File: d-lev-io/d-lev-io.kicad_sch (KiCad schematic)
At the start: 29 parts, among them J1 PJ-059A, J2 USB_C_Receptacle_USB2.0, J8 Conn_01x12_MountingPin, U1 AP1117-ADJ

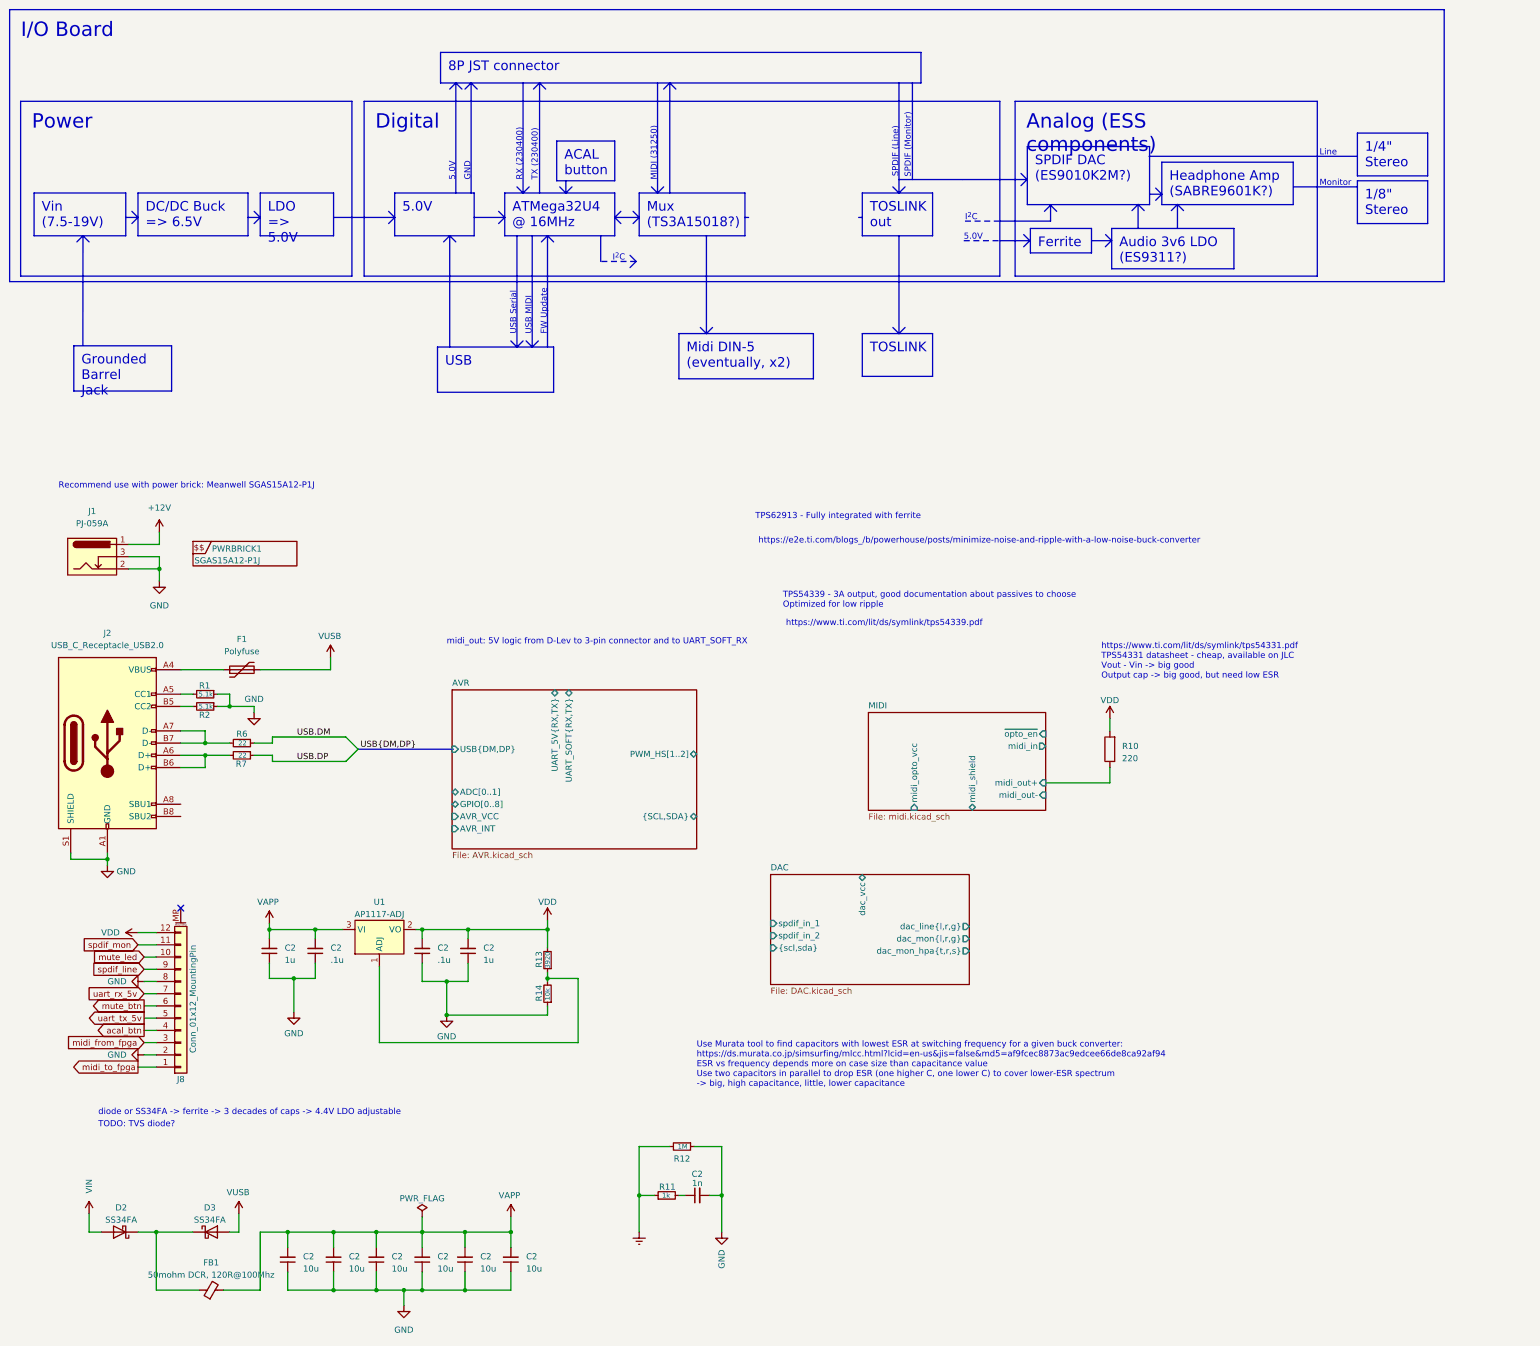
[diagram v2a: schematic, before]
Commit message: Add buck converter schematic
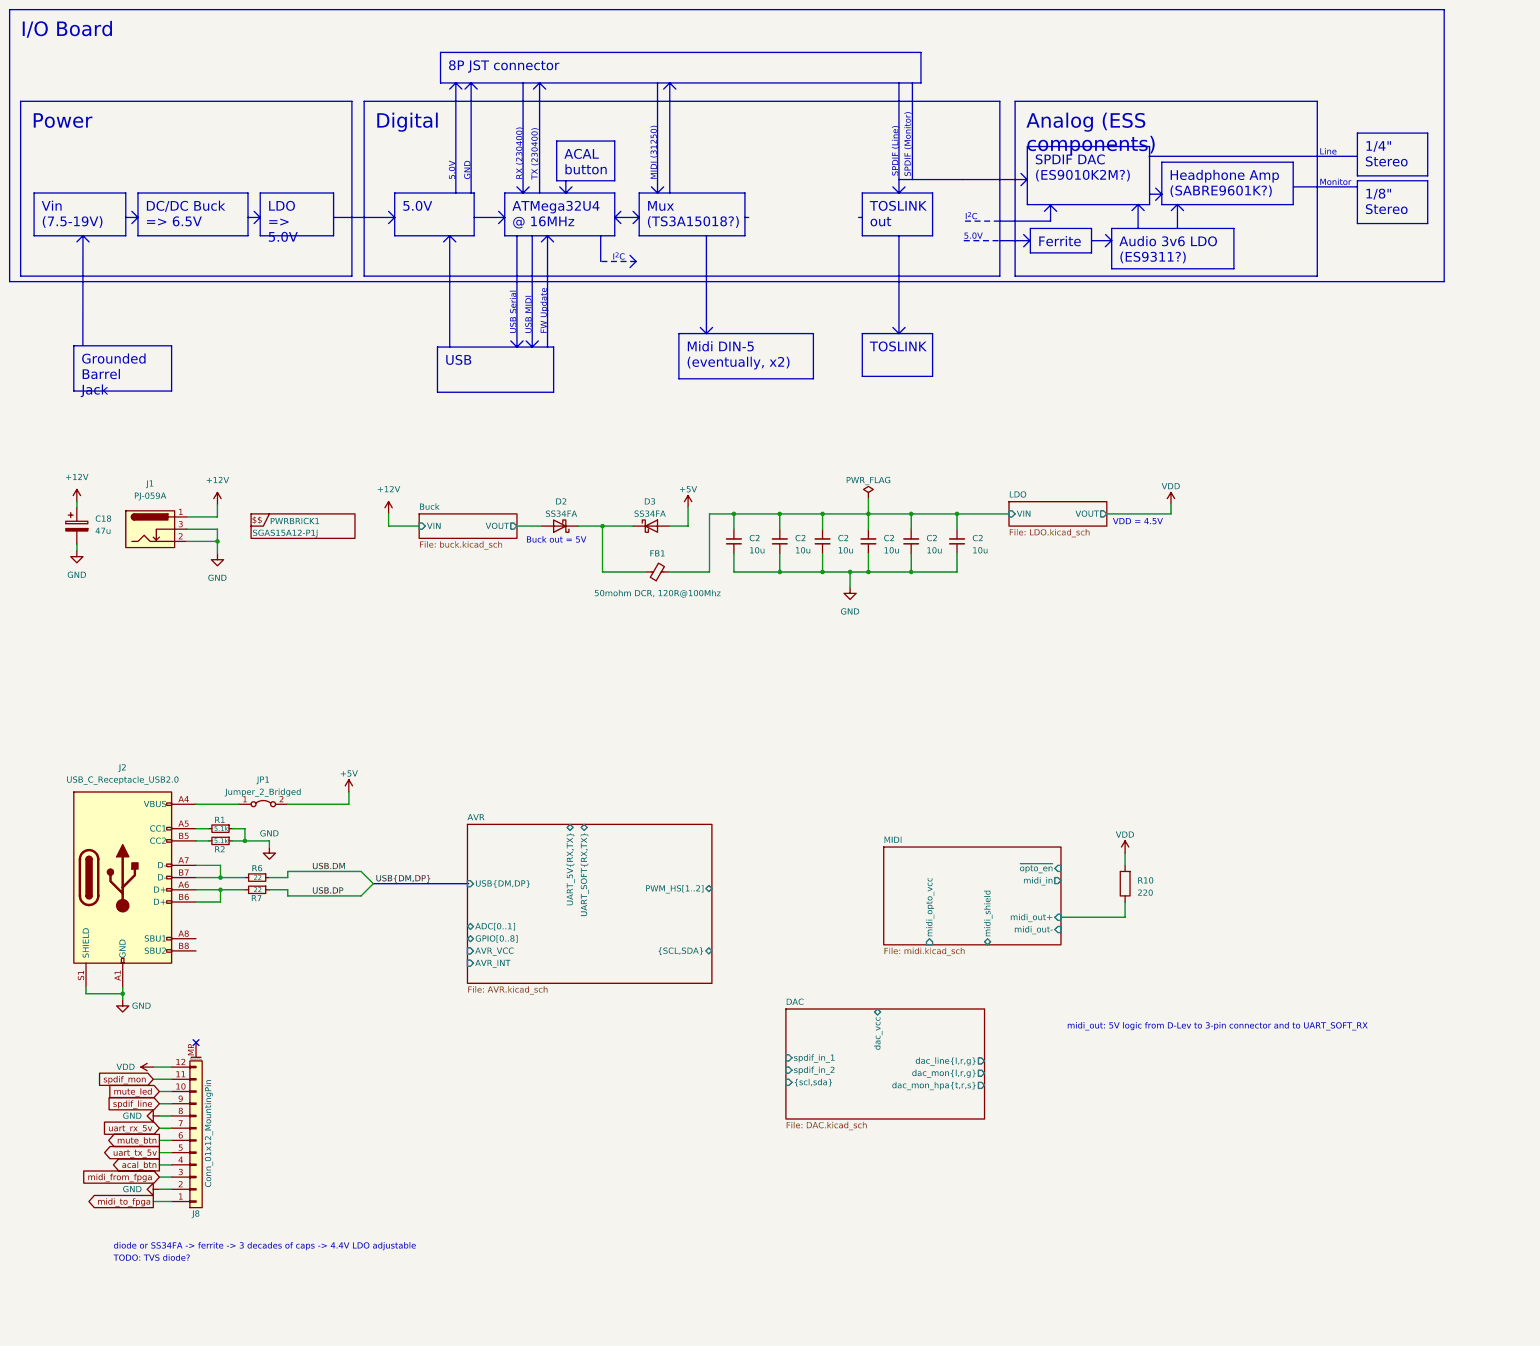
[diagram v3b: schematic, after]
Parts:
- removed C2 (x2): .1u, symbol Device:C_Small
- removed C2 (x2): 1u, symbol Device:C_Small
- removed C2: 1n, symbol Device:C_Small
- removed F1: Polyfuse, symbol Device:Polyfuse
- removed R11: 1k, Resistor_SMD:R_0805_2012Metric_Pad1.20x1.40mm_HandSolder, symbol Device:R_Small
- removed R12: 1M, Resistor_SMD:R_0805_2012Metric_Pad1.20x1.40mm_HandSolder, symbol Device:R_Small
- removed R13: 3920, Resistor_SMD:R_0805_2012Metric_Pad1.20x1.40mm_HandSolder, symbol Device:R_Small
- removed R14: 10k, Resistor_SMD:R_0805_2012Metric_Pad1.20x1.40mm_HandSolder, symbol Device:R_Small
- removed U1: AP1117-ADJ, Package_TO_SOT_SMD:SOT-223-3_TabPin2, symbol Regulator_Linear:AP1117-ADJ
- added C18: 47u, symbol Device:C_Polarized
- added JP1: Jumper_2_Bridged, symbol Jumper:Jumper_2_Bridged
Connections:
- net +12V: now also C18.1
- net +5V: now also D3.2 (A), JP1.2 (B); no longer D2.2 (A)
- net GND: now also C18.2
- net at J2.A4 (VBUS), J2.A9 (VBUS), J2.B4 (VBUS)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: now also JP1.1 (A)
- net VBUS renamed LDO/VIN
- net LDO/VIN: no longer D3.2 (A)
- new net Buck/VOUT: D2.2 (A)
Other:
- added sheet Buck (buck.kicad_sch)
- added sheet LDO (LDO.kicad_sch)
- note added: "Buck out = 5V"
- note added: "VDD = 4.5V"
- note removed: "Recommend use with power brick: Meanwell SGAS15A12-P1J"
- note removed: "TPS54339 - 3A output, good documentation about passives to choose Optimized for low ripple"
- note removed: "TPS62913 - Fully integrated with ferrite"
- note removed: "Use Murata tool to find capacitors with lowest ESR at switching frequency for a given buck converter: https://ds.murata.co.jp/simsurfing/mlcc.html?lcid=en-us&jis=false&md5=af9fcec8873ac9edcee66de8ca92af94 ESR vs frequency depends more on case size than capacitance value Use two capacitors in parallel to drop ESR (one higher C, one lower C) to cover lower-ESR spectrum -> big, high capacitance, lit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"
- note removed: "https://e2e.ti.com/blogs_/b/powerhouse/posts/minimize-noise-and-ripple-with-a-low-noise-buck-converter"
- note removed: "https://www.ti.com/lit/ds/symlink/tps54331.pdf TPS54331 datasheet - cheap, available on JLC Vout - Vin -> big good Output cap -> big good, but need low ESR"
- note removed: "https://www.ti.com/lit/ds/symlink/tps54339.pdf"
- moved on the sheet: C2, D2, D3, FB1, J1, J2, J8, PWRBRICK1, R1, R10, R2, R6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

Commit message: many many changes'
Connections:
- net midi_from_fpga renamed midi_from_fpga_3v
- net midi_to_fpga renamed midi_to_fpga_3v
- net uart_rx_5v renamed uart_rx_3v
- net uart_tx_5v renamed uart_tx_3v
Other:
- sheet LDO renamed LDO4V5
- added sheet LDO3v3 (LDO.kicad_sch)
- sheet AVR ports: added UART_AVR{RX,TX}; removed UART_5V{RX,TX}
- sheet LDO4V5: file LDO.kicad_sch -> LDO4v5.kicad_sch
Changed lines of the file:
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@@
   (junction (at 203.2 23.495) (diameter 0) (color 0 0 0 0)
+  )
+  (junction (at 247.65 23.495) (diameter 0) (color 0 0 0 0)
   )
   (junction (at 156.845 23.495) (diameter 0) (color 0 0 0 0)
@@
     (stroke (width 0) (type default))
   )
+  (wire (pts (xy 247.65 23.495) (xy 256.54 23.495))
+    (stroke (width 0) (type default))
+  )
   (wire (pts (xy 64.135 101.6) (xy 64.135 102.87))
     (stroke (width 0) (type default))
@@
     (stroke (width 0) (type dash))
   )
+  (wire (pts (xy 280.67 22.225) (xy 280.67 23.495))
+    (stroke (width 0) (type default))
+  )
   (wire (pts (xy 20.32 22.225) (xy 20.32 20.955))
     (stroke (width 0) (type default))
@@
   )
   (wire (pts (xy 234.315 23.495) (xy 247.65 23.495))
+    (stroke (width 0) (type default))
+  )
+  (wire (pts (xy 280.67 23.495) (xy 272.415 23.495))
     (stroke (width 0) (type default))
   )
@@
     )
   )
-  (global_label "midi_to_fpga" (shape output) (at 36.195 166.37 180) (fields_autoplaced)
+  (global_label "midi_to_fpga_3v" (shape output) (at 36.195 166.37 180) (fields_autoplaced)
     (effects (font (size 1.27 1.27)) (justify right))
-    (property "Intersheetrefs" "${INTERSHEET_REFS}" (at 22.5247 151.13 0)
+    (property "Intersheetrefs" "${INTERSHEET_REFS}" (at 18.11 166.37 0)
       (effects (font (size 1.27 1.27)) (justify right) hide)
     )
@@
     )
   )
-  (global_label "uart_tx_5v" (shape output) (at 37.465 156.21 180) (fields_autoplaced)
+  (global_label "uart_tx_3v" (shape output) (at 37.465 156.21 180) (fields_autoplaced)
     (effects (font (size 1.27 1.27)) (justify right))
-    (property "Intersheetrefs" "${INTERSHEET_REFS}" (at 24.8832 146.05 0)
+    (property "Intersheetrefs" "${INTERSHEET_REFS}" (at 24.8832 156.21 0)
       (effects (font (size 1.27 1.27)) (justify right) hide)
     )
   )
-  (global_label "uart_rx_5v" (shape input) (at 37.465 151.13 180) (fields_autoplaced)
+  (global_label "uart_rx_3v" (shape input) (at 37.465 151.13 180) (fields_autoplaced)
     (effects (font (size 1.27 1.27)) (justify right))
-    (property "Intersheetrefs" "${INTERSHEET_REFS}" (at 24.8227 143.51 0)
+    (property "Intersheetrefs" "${INTERSHEET_REFS}" (at 24.8227 151.13 0)
       (effects (font (size 1.27 1.27)) (justify right) hide)
     )
   )
-  (global_label "midi_from_fpga" (shape input) (at 37.465 161.29 180) (fields_autoplaced)
+  (global_label "midi_from_fpga_3v" (shape input) (at 37.465 161.29 180) (fields_autoplaced)
     (effects (font (size 1.27 1.27)) (justify right))
-    (property "Intersheetrefs" "${INTERSHEET_REFS}" (at 20.0452 148.59 0)
+    (property "Intersheetrefs" "${INTERSHEET_REFS}" (at 16.9005 161.29 0)
       (effects (font (size 1.27 1.27)) (justify right) hide)
     )
@@
     )
   )
+  (symbol (lib_id "power:+3V3") (at 280.67 22.225 0) (unit 1)
+    (in_bom yes) (on_board yes) (dnp no)
+    (property "Reference" "#PWR031" (at 280.67 26.035 0)
+      (effects (font (size 1.27 1.27)) hide)
+    )
+    (property "Value" "+3V3" (at 280.67 17.145 0)
+      (effects (font (size 1.27 1.27)))
+    )
+    (property "Footprint" "" (at 280.67 22.225 0)
+      (effects (font (size 1.27 1.27)) hide)
+    )
+    (property "Datasheet" "" (at 280.67 22.225 0)
+      (effects (font (size 1.27 1.27)) hide)
+    )
+    (pin "1")
+    (instances
+      (project "d-lev-io"
+        (path "/9261a07b-ae4a-4d72-8042-ea097cd0e5ed"
+          (reference "#PWR031") (unit 1)
+        )
+      )
+    )
+  )
   (symbol (lib_id "power:GND") (at 37.465 148.59 270) (unit 1)
     (in_bom yes) (on_board yes) (dnp no)
@@
     )
   )
+  (sheet (at 256.54 21.59) (size 15.875 3.81) (fields_autoplaced)
+    (stroke (width 0.1524) (type solid))
+    (fill (color 0 0 0 0.0000))
+    (property "Sheetname" "LDO3v3" (at 256.54 20.8784 0)
+      (effects (font (size 1.27 1.27)) (justify left bottom))
+    )
+    (property "Sheetfile" "LDO.kicad_sch" (at 256.54 25.9846 0)
+      (effects (font (size 1.27 1.27)) (justify left top))
+    )
+    (pin "VIN" input (at 256.54 23.495 180)
+      (effects (font (size 1.27 1.27)) (justify left))
+    )
+    (pin "VOUT" output (at 272.415 23.495 0)
+      (effects (font (size 1.27 1.27)) (justify right))
+    )
+    (instances
+      (project "d-lev-io"
+        (path "/9261a07b-ae4a-4d72-8042-ea097cd0e5ed" (page "8"))
+      )
+    )
+  )
   (sheet (at 101.473 88.011) (size 50.8 33.02) (fields_autoplaced)
     (stroke (width 0.1524) (type solid))
@@
       (effects (font (size 1.27 1.27)) (justify left))
     )
-    (pin "UART_5V{RX,TX}" bidirectional (at 122.809 88.011 90)
+    (pin "UART_AVR{RX,TX}" bidirectional (at 122.809 88.011 90)
       (effects (font (size 1.27 1.27)) (justify right))
     )
@@
     (stroke (width 0.1524) (type solid))
     (fill (color 0 0 0 0.0000))
-    (property "Sheetname" "LDO" (at 213.995 20.2434 0)
+    (property "Sheetname" "LDO4V5" (at 213.995 20.2434 0)
       (effects (font (size 1.27 1.27)) (justify left bottom))
     )
-    (property "Sheetfile" "LDO.kicad_sch" (at 213.995 26.6196 0)
+    (property "Sheetfile" "LDO4v5.kicad_sch" (at 213.995 26.6196 0)
       (effects (font (size 1.27 1.27)) (justify left top))
     )

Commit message: many more changes
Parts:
- removed R10: 220, Resistor_SMD:R_0603_1608Metric, symbol Device:R
- added J4: MIDI_OUT_JACK, Connector_Audio:Jack_3.5mm_CUI_SJ-3523-SMT_Horizontal, symbol Connector:AudioJack3
- added R18: 10, Resistor_SMD:R_0603_1608Metric, symbol Device:R_Small
- added R8: 33, Resistor_SMD:R_0603_1608Metric, symbol Device:R_Small
- added TP1: VIN, TestPoint:TestPoint_Pad_D1.5mm, symbol Connector:TestPoint
- added TP2: VUSB, TestPoint:TestPoint_Pad_D1.5mm, symbol Connector:TestPoint
- added TP3: VDD, TestPoint:TestPoint_Pad_D1.5mm, symbol Connector:TestPoint
- added TP4: VSYS, TestPoint:TestPoint_Pad_D1.5mm, symbol Connector:TestPoint
- added TP5: GND, TestPoint:TestPoint_Pad_D1.5mm, symbol Connector:TestPoint
- added U6: 74AHC1G126, Package_TO_SOT_SMD:SOT-23-5, symbol 74xGxx:74AHC1G126
- C1: renamed from C18; footprint (none) -> Capacitor_SMD:C_1206_3216Metric
- C2: footprint (none) -> Capacitor_SMD:C_0805_2012Metric
- D1: renamed from D2; footprint (none) -> Diode_SMD:D_SOD-123F
- D2: renamed from D3; footprint (none) -> Diode_SMD:D_SOD-123F
- FB1: footprint Inductor_SMD:L_0201_0603Metric -> Inductor_SMD:L_0603_1608Metric
- J3: renamed from J8; symbol Connector_Generic_MountingPin:Conn_01x12_MountingPin -> assorted:Conn_01x12_MountingPin
- JP1: footprint (none) -> Jumper:SolderJumper-2_P1.3mm_Bridged_RoundedPad1.0x1.5mm
- R1, R2: footprint Resistor_SMD:R_0805_2012Metric_Pad1.20x1.40mm_HandSolder -> Resistor_SMD:R_0603_1608Metric
- R3: renamed from R6; footprint Resistor_SMD:R_0805_2012Metric_Pad1.20x1.40mm_HandSolder -> Resistor_SMD:R_0603_1608Metric
- R4: renamed from R7; footprint Resistor_SMD:R_0805_2012Metric_Pad1.20x1.40mm_HandSolder -> Resistor_SMD:R_0603_1608Metric
- renumbered J2 to J1, J1 to J2
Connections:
- net LDO4V5/VIN is gone; now on net +5V: C2.2, C2.2, C2.2, C2.2, C2.2, C2.2, FB1.2
- net +12V: now also TP1.1
- net +3V3: now also R8.1, TP4.1, U6.1, U6.5 (VCC)
- net +5V: now also TP3.1; no longer D2.2 (A), JP1.2 (B)
- net GND: now also J4.S, TP5.1, U6.3 (GND)
- net midi_from_fpga_3v: now also U6.2
- new net: R18.1, U6.4
- new net: J4.R, R8.2
- new net: J4.T, R18.2
- new net VBUS: D2.2 (A), JP1.2 (B), TP2.1
- no-connect marks 1 -> 3
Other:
- removed sheet LDO4V5
- removed sheet MIDI
- sheet AVR ports: added PWM_16BIT[1..2], UART_AVR_RX, UART_AVR_SOFT_RX, UART_AVR_SOFT_TX, UART_AVR_TX; removed UART_AVR{RX,TX}, UART_SOFT{RX,TX}
- note added: "74 series 'little logic' cheat sheet: 74AHC -> 2.0-5.5v range, 8mA drive -> series resistors should be 33/10 ohm) 74AHCT -> 4.5-5.5v range, 8mA drive -> (VCC=5V, series resistors should be 220 ohm) 1G means 'one gate' 126 has OE, 125 has ~{OE}"
- note added: "Add LDO4v5.sch back in here if you decide you actually need it Big disadvantage here is that the 5V rail never actually goes through an LDO but do we care given that everything sensitive goes through its own LDO anyways? On bus power using any LDO between VBUS and 3v3 cuts our effective VDD to 3.8V worst case and runs all the LDOs in the circuit near dropout."
- note added: "TODO: add test points for every signal on both boards"
- note added: "todo: is 8mhz fast enough for AVR? Should we connect various i/o from the USB to the I/O controller for i.e. DAC control signaling? -> Yes, use cut/solder jumpers with sensible default states and make sure the in/out directions are well defined and no logic levels are crossed. Have the AVR toggle OE when it starts up but only after all the I/O ports are configured properly. What to do about MIDI_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"
- note removed: "TODO: TVS diode?"
- note removed: "midi_out: 5V logic from D-Lev to 3-pin connector and to UART_SOFT_RX"
- moved on the sheet: JP1
